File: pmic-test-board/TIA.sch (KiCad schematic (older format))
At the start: 10 parts

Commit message: more schematic capture
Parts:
- C401, C402, C403, C404: renamed from C?; footprint (none) -> Capacitor_SMD:C_0603_1608Metric
- R401, R402, R403, R404: renamed from R?; footprint (none) -> Resistor_SMD:R_0603_1608Metric
- gave numbers to parts that had none: 2
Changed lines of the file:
@@
 $EndDescr
 $Comp
-L wbraun_ic_lib:LMH6601 U?
+L wbraun_ic_lib:LMH6601 U401
 U 1 1 61A130A2
 P 2950 3800
-F 0 "U?" H 3100 3950 50  0000 L CNN
+F 0 "U401" H 3100 3950 50  0000 L CNN
 F 1 "LMH6601" H 3150 3650 50  0000 L CNN
 F 2 "Package_TO_SOT_SMD:TSOT-23-6" H 3050 3550 50  0001 L CNN
@@
 $EndComp
 $Comp
-L Device:R R?
+L Device:R R401
 U 1 1 61A13740
 P 1850 4500
-F 0 "R?" H 1920 4546 50  0000 L CNN
+F 0 "R401" H 1920 4546 50  0000 L CNN
 F 1 "1k" H 1920 4455 50  0000 L CNN
-F 2 "" V 1780 4500 50  0001 C CNN
+F 2 "Resistor_SMD:R_0603_1608Metric" V 1780 4500 50  0001 C CNN
 F 3 "~" H 1850 4500 50  0001 C CNN
 	1    1850 4500
@@
 $EndComp
 $Comp
-L Device:R R?
+L Device:R R402
 U 1 1 61A13D16
 P 1850 4950
-F 0 "R?" H 1920 4996 50  0000 L CNN
+F 0 "R402" H 1920 4996 50  0000 L CNN
 F 1 "1k" H 1920 4905 50  0000 L CNN
-F 2 "" V 1780 4950 50  0001 C CNN
+F 2 "Resistor_SMD:R_0603_1608Metric" V 1780 4950 50  0001 C CNN
 F 3 "~" H 1850 4950 50  0001 C CNN
 	1    1850 4950
@@
 $EndComp
 $Comp
-L Device:C C?
+L Device:C C402
 U 1 1 61A14161
 P 2300 5000
-F 0 "C?" H 2415 5046 50  0000 L CNN
+F 0 "C402" H 2415 5046 50  0000 L CNN
 F 1 "0.1u" H 2415 4955 50  0000 L CNN
-F 2 "" H 2338 4850 50  0001 C CNN
+F 2 "Capacitor_SMD:C_0603_1608Metric" H 2338 4850 50  0001 C CNN
 F 3 "~" H 2300 5000 50  0001 C CNN
 	1    2300 5000
@@
 $EndComp
 $Comp
-L Device:C C?
+L Device:C C404
 U 1 1 61A14995
 P 4050 3000
-F 0 "C?" H 4165 3046 50  0000 L CNN
+F 0 "C404" H 4165 3046 50  0000 L CNN
 F 1 "4.7u" H 4165 2955 50  0000 L CNN
-F 2 "" H 4088 2850 50  0001 C CNN
+F 2 "Capacitor_SMD:C_0603_1608Metric" H 4088 2850 50  0001 C CNN
 F 3 "~" H 4050 3000 50  0001 C CNN
 	1    4050 3000
@@
 $EndComp
 $Comp
-L Device:R R?
+L Device:R R404
 U 1 1 61A14E3A
 P 2900 3300
-F 0 "R?" V 2693 3300 50  0000 C CNN
+F 0 "R404" V 2693 3300 50  0000 C CNN
 F 1 "R" V 2784 3300 50  0000 C CNN
-F 2 "" V 2830 3300 50  0001 C CNN
+F 2 "Resistor_SMD:R_0603_1608Metric" V 2830 3300 50  0001 C CNN
 F 3 "~" H 2900 3300 50  0001 C CNN
 	1    2900 3300
@@
 $EndComp
 $Comp
-L Device:C C?
+L Device:C C403
 U 1 1 61A15354
 P 2900 2900
-F 0 "C?" V 2648 2900 50  0000 C CNN
+F 0 "C403" V 2648 2900 50  0000 C CNN
 F 1 "C" V 2739 2900 50  0000 C CNN
-F 2 "" H 2938 2750 50  0001 C CNN
+F 2 "Capacitor_SMD:C_0603_1608Metric" H 2938 2750 50  0001 C CNN
 F 3 "~" H 2900 2900 50  0001 C CNN
 	1    2900 2900
@@
 $EndComp
 $Comp
-L power:GND #PWR?
+L power:GND #PWR0187
 U 1 1 61A168C1
 P 2850 4200
-F 0 "#PWR?" H 2850 3950 50  0001 C CNN
+F 0 "#PWR0187" H 2850 3950 50  0001 C CNN
 F 1 "GND" H 2855 4027 50  0000 C CNN
 F 2 "" H 2850 4200 50  0001 C CNN
@@
 	2950 4100 3100 4100
 $Comp
-L power:+3.3VA #PWR?
+L power:+3.3VA #PWR0188
 U 1 1 61A17330
 P 3100 4100
-F 0 "#PWR?" H 3100 3950 50  0001 C CNN
+F 0 "#PWR0188" H 3100 3950 50  0001 C CNN
 F 1 "+3.3VA" V 3115 4228 50  0000 L CNN
 F 2 "" H 3100 4100 50  0001 C CNN
@@
 $EndComp
 $Comp
-L power:+3.3VA #PWR?
+L power:+3.3VA #PWR0189
 U 1 1 61A17BE8
 P 2900 3500
-F 0 "#PWR?" H 2900 3350 50  0001 C CNN
+F 0 "#PWR0189" H 2900 3350 50  0001 C CNN
 F 1 "+3.3VA" V 2915 3628 50  0000 L CNN
 F 2 "" H 2900 3500 50  0001 C CNN
@@
 Connection ~ 2400 3300
 $Comp
-L power:+3.3VA #PWR?
+L power:+3.3VA #PWR0190
 U 1 1 61A19E21
 P 4050 2800
-F 0 "#PWR?" H 4050 2650 50  0001 C CNN
+F 0 "#PWR0190" H 4050 2650 50  0001 C CNN
 F 1 "+3.3VA" H 4065 2973 50  0000 C CNN
 F 2 "" H 4050 2800 50  0001 C CNN
@@
 $EndComp
 $Comp
-L power:GND #PWR?
+L power:GND #PWR0191
 U 1 1 61A1A5F5
 P 4050 3200
-F 0 "#PWR?" H 4050 2950 50  0001 C CNN
+F 0 "#PWR0191" H 4050 2950 50  0001 C CNN
 F 1 "GND" H 4055 3027 50  0000 C CNN
 F 2 "" H 4050 3200 50  0001 C CNN
@@
 	2300 5250 2300 5150
 $Comp
-L power:GND #PWR?
+L power:GND #PWR0192
 U 1 1 61A1B12C
 P 1850 5250
-F 0 "#PWR?" H 1850 5000 50  0001 C CNN
+F 0 "#PWR0192" H 1850 5000 50  0001 C CNN
 F 1 "GND" H 1855 5077 50  0000 C CNN
 F 2 "" H 1850 5250 50  0001 C CNN
@@
 	1850 4750 1850 4800
 $Comp
-L power:+3.3VA #PWR?
+L power:+3.3VA #PWR0193
 U 1 1 61A1BAC3
 P 1850 4300
-F 0 "#PWR?" H 1850 4150 50  0001 C CNN
+F 0 "#PWR0193" H 1850 4150 50  0001 C CNN
 F 1 "+3.3VA" H 1865 4473 50  0000 C CNN
 F 2 "" H 1850 4300 50  0001 C CNN
@@
 TIA_VREF
 $Comp
-L Device:R R?
+L Device:R R403
 U 1 1 61A1CC7D
 P 1950 2900
-F 0 "R?" V 1743 2900 50  0000 C CNN
+F 0 "R403" V 1743 2900 50  0000 C CNN
 F 1 "DNP" V 1834 2900 50  0000 C CNN
-F 2 "" V 1880 2900 50  0001 C CNN
+F 2 "Resistor_SMD:R_0603_1608Metric" V 1880 2900 50  0001 C CNN
 F 3 "~" H 1950 2900 50  0001 C CNN
 	1    1950 2900
@@
 $EndComp
 $Comp
-L Device:C C?
+L Device:C C401
 U 1 1 61A1D8A3
 P 1950 3300
-F 0 "C?" V 1698 3300 50  0000 C CNN
+F 0 "C401" V 1698 3300 50  0000 C CNN
 F 1 "DNP" V 1789 3300 50  0000 C CNN
-F 2 "" H 1988 3150 50  0001 C CNN
+F 2 "Capacitor_SMD:C_0603_1608Metric" H 1988 3150 50  0001 C CNN
 F 3 "~" H 1950 3300 50  0001 C CNN
 	1    1950 3300
@@
 Connection ~ 2400 2900
 $Comp
-L power:GND #PWR?
+L power:GND #PWR0194
 U 1 1 61A1E556
 P 1650 3300
-F 0 "#PWR?" H 1650 3050 50  0001 C CNN
+F 0 "#PWR0194" H 1650 3050 50  0001 C CNN
 F 1 "GND" V 1655 3172 50  0000 R CNN
 F 2 "" H 1650 3300 50  0001 C CNN
@@
 	1750 3300 1800 3300
 $Comp
-L Connector:Conn_01x02_Male J?
+L Connector:Conn_01x02_Male J401
 U 1 1 61A1FAB6
 P 4350 3900
-F 0 "J?" H 4322 3782 50  0000 R CNN
+F 0 "J401" H 4322 3782 50  0000 R CNN
 F 1 "Conn_01x02_Male" H 4322 3873 50  0000 R CNN
 F 2 "" H 4350 3900 50  0001 C CNN

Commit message: PCB routing done
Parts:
- added FB401: Ferrite_Bead_Small, Inductor_SMD:L_0805_2012Metric, symbol Device:Ferrite_Bead_Small
- added TP401: TestPoint, wbraun_smd:THM_COMPACT, symbol Connector:TestPoint
- J401: footprint (none) -> Connector_PinHeader_2.54mm:PinHeader_1x02_P2.54mm_Vertical
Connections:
- net GND: now also TP401.1
- net +3.3VA renamed TIA_3V3
- net TIA_3V3: now also FB401.1
- new net +3V3: FB401.2
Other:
- moved on the sheet: C401, C402, C403, C404, J401, R401, R402, R403, R404, U401

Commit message: schematic review and gerber generation
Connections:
- net IMON: now also U401.4 (-); no longer U401.3 (+)
- net TIA_VREF: now also U401.3 (+); no longer U401.4 (-)
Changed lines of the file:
@@
 	3650 3200 3650 3600
-Wire Wire Line
-	3650 3600 3900 3600
 Wire Wire Line
 	4000 2800 3650 2800
@@
 Wire Wire Line
 	3100 4200 3100 4250
-Wire Wire Line
-	3550 4650 3550 3800
-Wire Wire Line
-	3550 3800 3900 3800
-Connection ~ 3550 4650
 Text Label 3550 4650 0    50   ~ 0
 TIA_VREF
@@
 Wire Wire Line
 	3650 3600 3200 3600
-Connection ~ 3650 3600
 Text Label 4950 3700 0    50   ~ 0
 TIA_SENSE
@@
 Text Label 4350 4000 0    50   ~ 0
 TIA_3V3
+Wire Wire Line
+	3650 3600 3650 3800
+Wire Wire Line
+	3650 3800 3900 3800
+Connection ~ 3650 3600
+Wire Wire Line
+	3550 4650 3550 4050
+Wire Wire Line
+	3550 4050 3800 4050
+Wire Wire Line
+	3800 4050 3800 3600
+Wire Wire Line
+	3800 3600 3900 3600
+Connection ~ 3550 4650
 $EndSCHEMATC

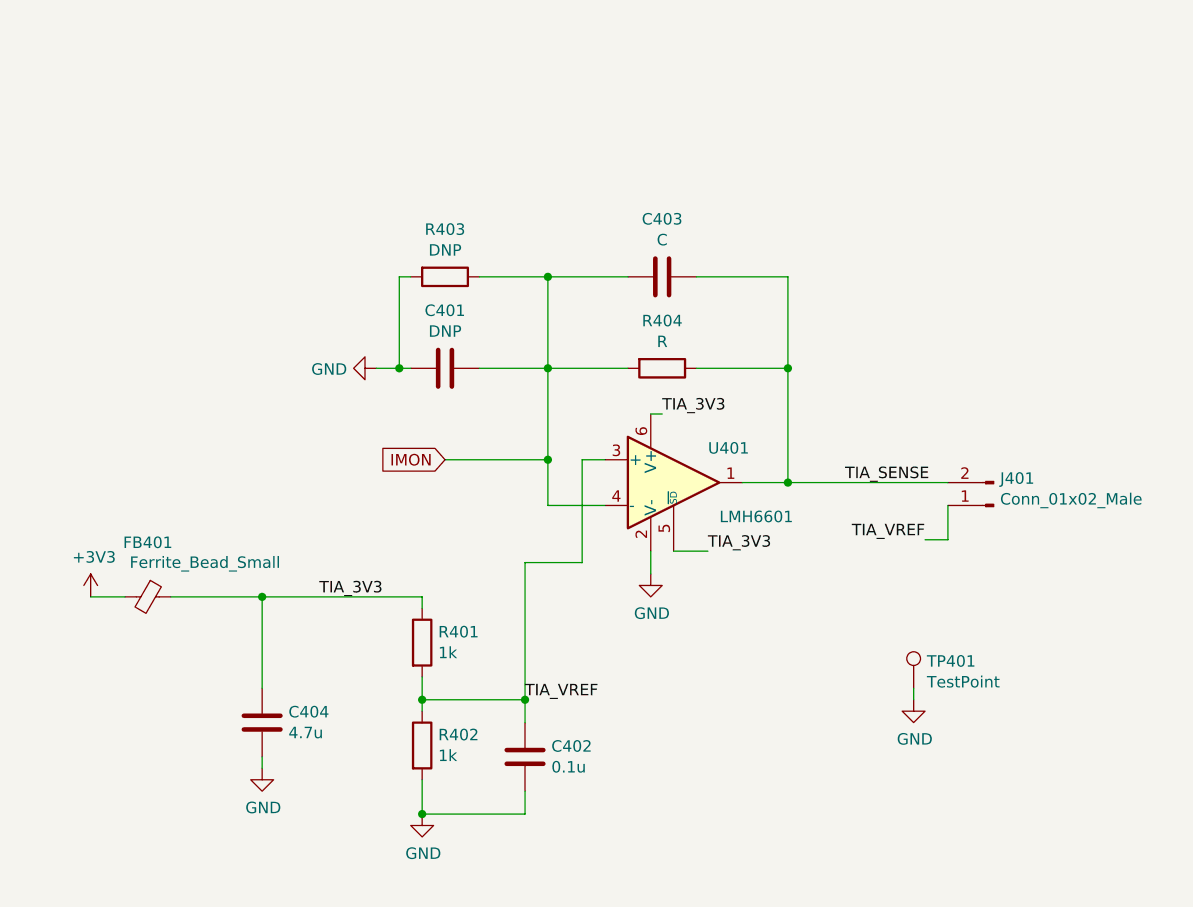
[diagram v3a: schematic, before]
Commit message: added test firmware and test results
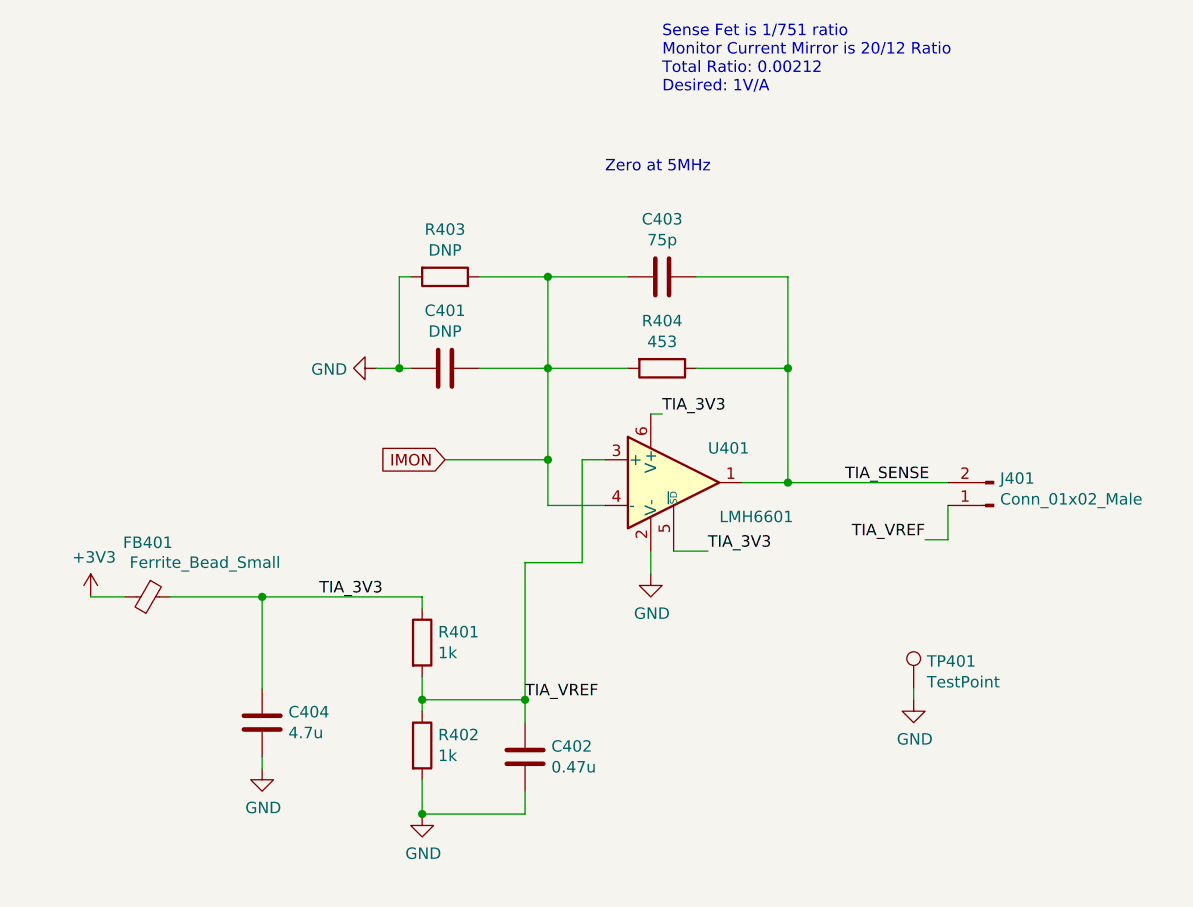
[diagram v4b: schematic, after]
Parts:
- C402: value 0.1u -> 0.47u; MPN (none) -> CL10B474KO8NFNC
- C403: value C -> 75p; MPN (none) -> CC0603JRNPO9BN750
- C404: MPN (none) -> CL10A475MO8NNNC
- FB401: MPN (none) -> 742792012
- R401, R402: MPN (none) -> RMCF0603FG1K00
- R404: value R -> 453; MPN (none) -> CRCW0603453RFKEA
- TP401: MPN (none) -> 5119
- U401: MPN (none) -> LMH6601MG/NOPB
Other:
- note added: "Sense Fet is 1/751 ratio\nMonitor Current Mirror is 20/12 Ratio\nTotal Ratio: 0.00212\nDesired: 1V/A"
- note added: "Zero at 5MHz"
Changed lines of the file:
@@
 F 2 "Package_TO_SOT_SMD:TSOT-23-6" H 4300 3450 50  0001 L CNN
 F 3 "http://www.ti.com/lit/ds/symlink/lmh6612.pdf" H 4350 3850 50  0001 C CNN
+F 4 "LMH6601MG/NOPB" H 4200 3700 50  0001 C CNN "MPN"
 	1    4200 3700
 	1    0    0    -1
@@
 F 2 "Resistor_SMD:R_0603_1608Metric" V 3030 4400 50  0001 C CNN
 F 3 "~" H 3100 4400 50  0001 C CNN
+F 4 "RMCF0603FG1K00" H 3100 4400 50  0001 C CNN "MPN"
 	1    3100 4400
 	1    0    0    -1
@@
 F 2 "Resistor_SMD:R_0603_1608Metric" V 3030 4850 50  0001 C CNN
 F 3 "~" H 3100 4850 50  0001 C CNN
+F 4 "RMCF0603FG1K00" H 3100 4850 50  0001 C CNN "MPN"
 	1    3100 4850
 	1    0    0    -1
@@
 P 3550 4900
 F 0 "C402" H 3665 4946 50  0000 L CNN
-F 1 "0.1u" H 3665 4855 50  0000 L CNN
+F 1 "0.47u" H 3665 4855 50  0000 L CNN
 F 2 "Capacitor_SMD:C_0603_1608Metric" H 3588 4750 50  0001 C CNN
 F 3 "~" H 3550 4900 50  0001 C CNN
+F 4 "CL10B474KO8NFNC" H 3550 4900 50  0001 C CNN "MPN"
 	1    3550 4900
 	1    0    0    -1
@@
 F 2 "Capacitor_SMD:C_0603_1608Metric" H 2438 4600 50  0001 C CNN
 F 3 "~" H 2400 4750 50  0001 C CNN
+F 4 "CL10A475MO8NNNC" H 2400 4750 50  0001 C CNN "MPN"
 	1    2400 4750
 	1    0    0    -1
@@
 P 4150 3200
 F 0 "R404" V 3943 3200 50  0000 C CNN
-F 1 "R" V 4034 3200 50  0000 C CNN
+F 1 "453" V 4034 3200 50  0000 C CNN
 F 2 "Resistor_SMD:R_0603_1608Metric" V 4080 3200 50  0001 C CNN
 F 3 "~" H 4150 3200 50  0001 C CNN
+F 4 "CRCW0603453RFKEA" V 4150 3200 50  0001 C CNN "MPN"
 	1    4150 3200
 	0    1    1    0
@@
 P 4150 2800
 F 0 "C403" V 3898 2800 50  0000 C CNN
-F 1 "C" V 3989 2800 50  0000 C CNN
+F 1 "75p" V 3989 2800 50  0000 C CNN
 F 2 "Capacitor_SMD:C_0603_1608Metric" H 4188 2650 50  0001 C CNN
 F 3 "~" H 4150 2800 50  0001 C CNN
+F 4 "CC0603JRNPO9BN750" V 4150 2800 50  0001 C CNN "MPN"
 	1    4150 2800
 	0    1    1    0
@@
 F 2 "wbraun_smd:THM_COMPACT" H 5450 4600 50  0001 C CNN
 F 3 "~" H 5450 4600 50  0001 C CNN
+F 4 "5119" H 5250 4600 50  0001 C CNN "MPN"
 	1    5250 4600
 	1    0    0    -1
@@
 F 2 "Inductor_SMD:L_0805_2012Metric" V 1830 4200 50  0001 C CNN
 F 3 "~" H 1900 4200 50  0001 C CNN
+F 4 "742792012" H 1900 4200 50  0001 C CNN "MPN"
 	1    1900 4200
 	0    1    1    0
@@
 	3800 3600 3900 3600
 Connection ~ 3550 4650
+Text Notes 4150 2000 0    50   ~ 0
+Sense Fet is 1/751 ratio\nMonitor Current Mirror is 20/12 Ratio\nTotal Ratio: 0.00212\nDesired: 1V/A
+Text Notes 3900 2350 0    50   ~ 0
+Zero at 5MHz
 $EndSCHEMATC
